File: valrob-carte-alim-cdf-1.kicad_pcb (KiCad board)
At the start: 4 copper layers, 87 x 57 mm, 201 parts, among them J1 USB_C_Receptacle_USB2.0_14P, J10 Conn_01x02, J11 Conn_01x02, J12 Conn_01x02, J13 Conn_01x02, J14 Conn_01x02, J15 Conn_01x02, J16 Conn_01x02, J17 Conn_01x02, J18 Conn_01x02, J19 Conn_01x02, J2 Conn_01x02, J20 Conn_01x02, J21 Conn_01x02, J22 Conn_01x02, J3 Conn_01x04_Pin, J4 Conn_01x02, J5 Conn_01x02, J6 Conn_01x02, J7 Conn_01x02, J8 Conn_01x02, J9 Conn_01x02, SW1 SW_Push, SW2 SW_Push, SW3 SW_Push, U1 SN65HVD230, U10 TPS259472A, U11 TPS259472A, U12 TPS259472A, U2 ESP32-S3-WROOM-1, U3 TLV75733PDBV, U4 TPS56A37, U5 TPS56A37, U6 TPS259472A, U7 TPS259472A, U8 TPS259472A, U9 TPS259472A

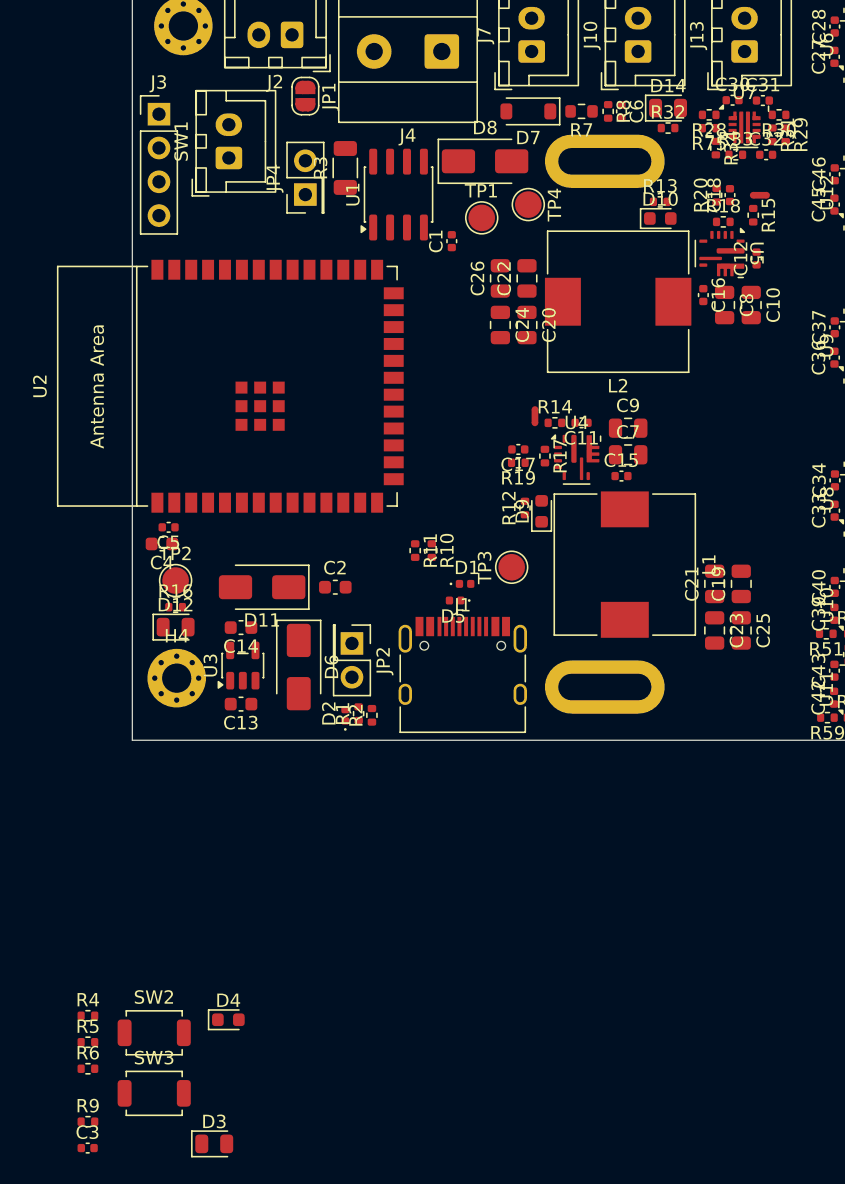
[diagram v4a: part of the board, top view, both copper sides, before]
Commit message: pcb: finish initial layout
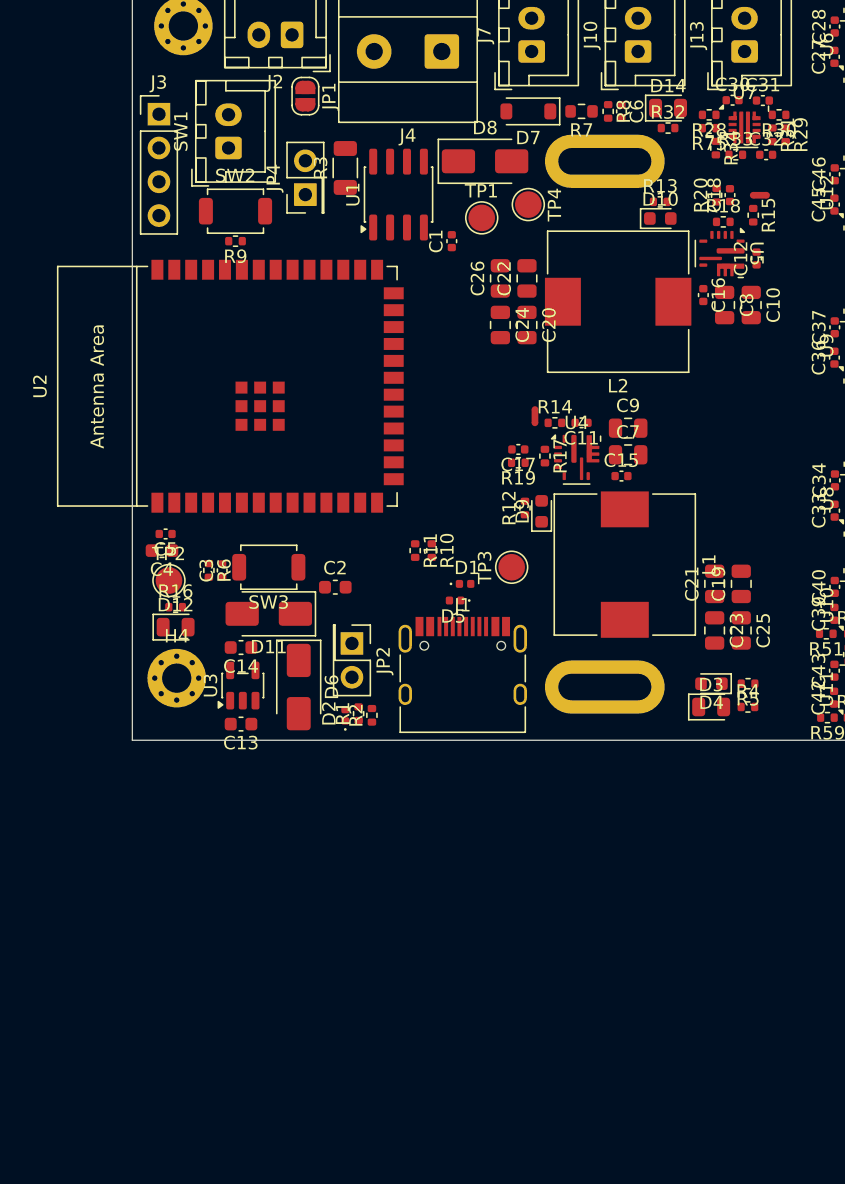
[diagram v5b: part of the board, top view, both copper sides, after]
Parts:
- moved R9 67.1 mm to (97.8, 72.5), turned to 180 degrees
- moved SW2 62.0 mm to (97.8, 70.2)
- moved R5 56.4 mm to (136.3, 105.8), turned to 180 degrees
- moved R4 54.7 mm to (136.2, 107.5)
- moved D3 49.7 mm to (133.5, 107.5)
- moved C3 44.6 mm to (96.8, 97.2), turned to 90 degrees
- moved D4 44.2 mm to (133.5, 105.8), turned to 180 degrees
- moved SW3 40.5 mm to (100.2, 97.0), turned to 180 degrees
- moved R6 38.5 mm to (95.8, 97.2), turned to -90 degrees
- moved D11 2.06 mm to (100.2, 100.5)
- moved C13 1.50 mm to (98.2, 108.8)
- moved C14 1.50 mm to (98.2, 103.0)
- moved D6 1.50 mm to (102.5, 106.0)
- moved U3 1.50 mm to (98.3, 105.9)
- moved SW1 0.75 mm to (97.2, 65.5)
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
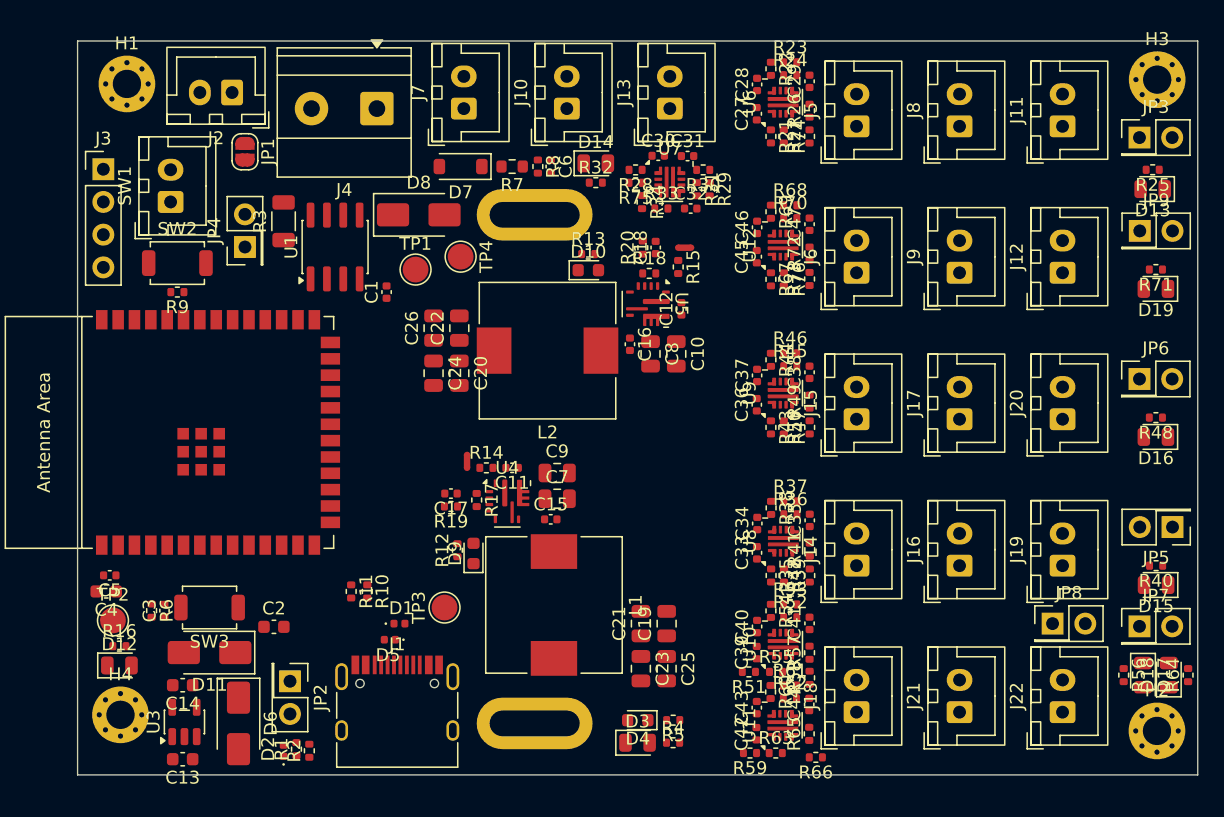
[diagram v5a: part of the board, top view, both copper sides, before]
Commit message: pcb: line up 2.54 headers
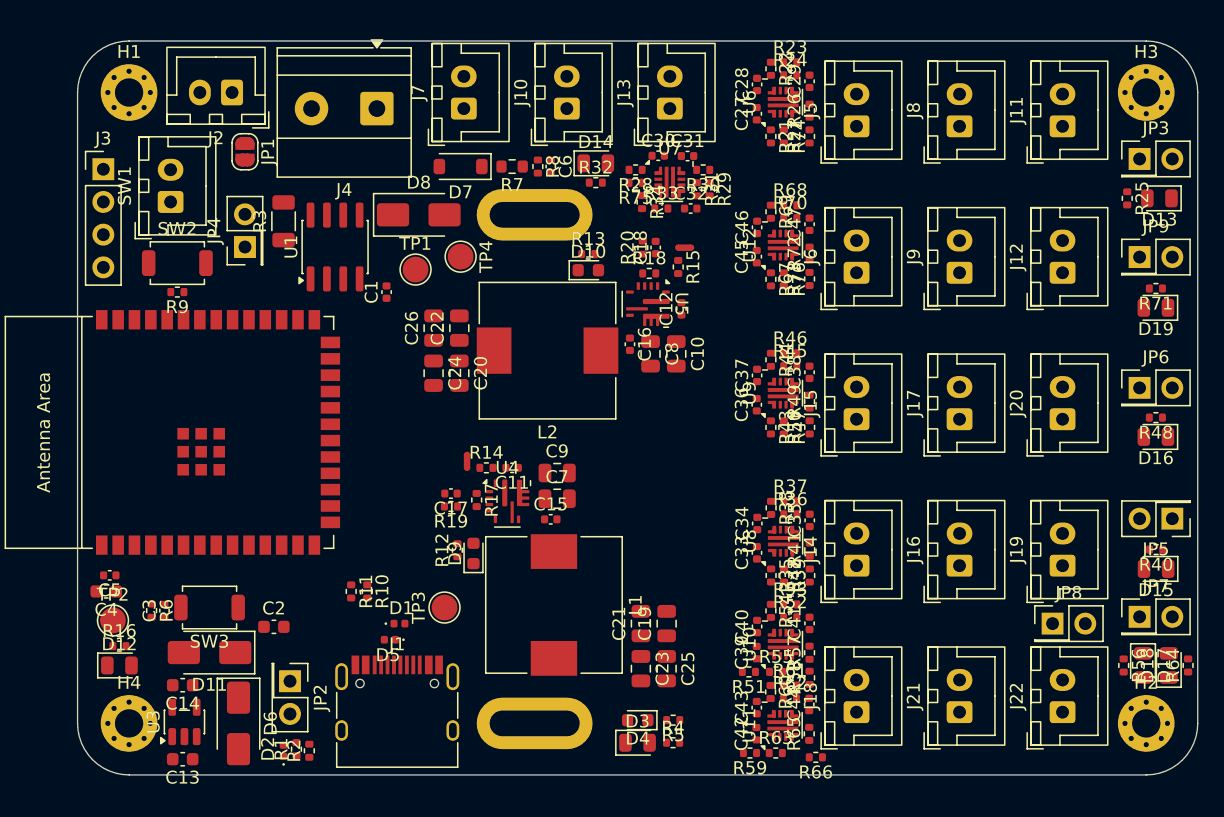
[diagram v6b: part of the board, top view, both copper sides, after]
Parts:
- moved R25 2.97 mm to (171.5, 65.2), turned to -90 degrees
- moved JP9 2.03 mm to (172.5, 69.8)
- moved JP3 1.66 mm to (172.5, 62.2)
- moved D19 1.47 mm to (173.8, 73.7)
- moved R71 1.47 mm to (173.8, 72.2)
- moved H3 1.31 mm to (173.0, 57.0)
- moved D15 1.25 mm to (173.8, 94.0)
- moved R40 1.25 mm to (173.8, 92.5)
- moved H2 1.02 mm to (173.0, 106.0)
- moved H4 0.94 mm to (94.0, 106.0)
- moved D13 0.89 mm to (174.0, 65.2)
- moved D17 0.75 mm to (172.8, 101.5)
- moved D18 0.75 mm to (174.8, 101.5)
- moved R56 0.75 mm to (171.2, 101.5)
- moved R64 0.75 mm to (176.2, 101.5)
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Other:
- outline, holes or cut-outs redrawn
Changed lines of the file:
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@@
 	(footprint "Resistor_SMD:R_0402_1005Metric"
 		(layer "F.Cu")
-		(at 173.765 93.75 180)
+		(at 173.765 92.5 180)
 		(descr "Resistor SMD 0402 (1005 Metric), square (rectangular) end terminal, IPC-7351 nominal, (Body size source: IPC-SM-782 page 72, https://www.pcb-3d.com/wordpress/wp-content/uploads/ipc-sm-782a_amendment_1_and_2.pdf), generated with kicad-footprint-generator")
 		(tags "resistor")
@@
 	(footprint "MountingHole:MountingHole_2.2mm_M2_Pad_Via"
 		(layer "F.Cu")
-		(at 173.85 56)
+		(at 173 57)
 		(descr "Mounting Hole 2.2mm, M2, generated by kicad-footprint-generator mountinghole.py")
 		(tags "mountinghole M2")
@@
 	(footprint "Connector_PinHeader_2.54mm:PinHeader_2x01_P2.54mm_Vertical"
 		(layer "F.Cu")
-		(at 172.475 79.25)
+		(at 172.484558 79.941668)
 		(descr "Through hole straight pin header, 2x01, 2.54mm pitch, double rows")
 		(tags "Through hole pin header THT 2x01 2.54mm double row")
@@
 	(footprint "LED_SMD:LED_0805_2012Metric"
 		(layer "F.Cu")
-		(at 173.5 64.5 180)
+		(at 174.024558 65.221668 180)
 		(descr "LED SMD 0805 (2012 Metric), square (rectangular) end terminal, IPC-7351 nominal, (Body size source: https://docs.google.com/spreadsheets/d/1BsfQQcO9C6DZCsRaXUlFlo91Tg2WpOkGARC1WS5S8t0/edit?usp=sharing), generated with kicad-footprint-generator")
 		(tags "LED")
@@
 	(footprint "Resistor_SMD:R_0402_1005Metric"
 		(layer "F.Cu")
-		(at 176.25 102.25 90)
+		(at 176.25 101.5 90)
 		(descr "Resistor SMD 0402 (1005 Metric), square (rectangular) end terminal, IPC-7351 nominal, (Body size source: IPC-SM-782 page 72, https://www.pcb-3d.com/wordpress/wp-content/uploads/ipc-sm-782a_amendment_1_and_2.pdf), generated with kicad-footprint-generator")
 		(tags "resistor")
@@
 	(footprint "LED_SMD:LED_0805_2012Metric"
 		(layer "F.Cu")
-		(at 173.765 95.25 180)
+		(at 173.765 94 180)
 		(descr "LED SMD 0805 (2012 Metric), square (rectangular) end terminal, IPC-7351 nominal, (Body size source: https://docs.google.com/spreadsheets/d/1BsfQQcO9C6DZCsRaXUlFlo91Tg2WpOkGARC1WS5S8t0/edit?usp=sharing), generated with kicad-footprint-generator")
 		(tags "LED")
@@
 	(footprint "MountingHole:MountingHole_2.2mm_M2_Pad_Via"
 		(layer "F.Cu")
-		(at 93.333274 105.333274)
+		(at 94 106)
 		(descr "Mounting Hole 2.2mm, M2, generated by kicad-footprint-generator mountinghole.py")
 		(tags "mountinghole M2")
@@
 	(footprint "LED_SMD:LED_0805_2012Metric"
 		(layer "F.Cu")
-		(at 173.75 72.25 180)
+		(at 173.75 73.721668 180)
 		(descr "LED SMD 0805 (2012 Metric), square (rectangular) end terminal, IPC-7351 nominal, (Body size source: https://docs.google.com/spreadsheets/d/1BsfQQcO9C6DZCsRaXUlFlo91Tg2WpOkGARC1WS5S8t0/edit?usp=sharing), generated with kicad-footprint-generator")
 		(tags "LED")
@@
 	(footprint "Connector_PinHeader_2.54mm:PinHeader_2x01_P2.54mm_Vertical"
 		(layer "F.Cu")
-		(at 172.475 98.46)
+		(at 172.484558 97.721668)
 		(descr "Through hole straight pin header, 2x01, 2.54mm pitch, double rows")
 		(tags "Through hole pin header THT 2x01 2.54mm double row")
@@
 	(footprint "LED_SMD:LED_0805_2012Metric"
 		(layer "F.Cu")
-		(at 174.75 102.25 90)
+		(at 174.75 101.5 90)
 		(descr "LED SMD 0805 (2012 Metric), square (rectangular) end terminal, IPC-7351 nominal, (Body size source: https://docs.google.com/spreadsheets/d/1BsfQQcO9C6DZCsRaXUlFlo91Tg2WpOkGARC1WS5S8t0/edit?usp=sharing), generated with kicad-footprint-generator")
 		(tags "LED")
@@
 	(footprint "Resistor_SMD:R_0402_1005Metric"
 		(layer "F.Cu")
-		(at 173.5 63 180)
+		(at 171.524558 65.221668 -90)
 		(descr "Resistor SMD 0402 (1005 Metric), square (rectangular) end terminal, IPC-7351 nominal, (Body size source: IPC-SM-782 page 72, https://www.pcb-3d.com/wordpress/wp-content/uploads/ipc-sm-782a_amendment_1_and_2.pdf), generated with kicad-footprint-generator")
 		(tags "resistor")
 		(property "Reference" "R25"
-			(at 0 -1.17 0)
+			(at 0 -1.17 90)
 			(layer "F.SilkS")
 			(effects
@@
 		)
 		(property "Value" "5k1"
-			(at 0 1.17 0)
+			(at 0 1.17 90)
 			(layer "F.Fab")
 			(effects
@@
 		)
 		(property "Datasheet" "~"
-			(at 0 0 0)
+			(at 0 0 90)
 			(layer "F.Fab")
 			(hide yes)
@@
 		)
 		(property "Description" "Resistor"
-			(at 0 0 0)
+			(at 0 0 90)
 			(layer "F.Fab")
 			(hide yes)
@@
 		)
 		(property "Manufacturer" "Uniroyal Elec"
-			(at 0 0 180)
+			(at 0 0 270)
 			(unlocked yes)
 			(layer "F.Fab")
@@
 		)
 		(property "Manufacturer Part Number" "0402WGF5101TCE"
-			(at 0 0 180)
+			(at 0 0 270)
 			(unlocked yes)
 			(layer "F.Fab")
@@
 		)
 		(property "Basic" "Y"
-			(at 0 0 180)
+			(at 0 0 270)
 			(unlocked yes)
 			(layer "F.Fab")
@@
 		)
 		(property "JLCPCB Part #" "C25905"
-			(at 0 0 180)
+			(at 0 0 270)
 			(unlocked yes)
 			(layer "F.Fab")
@@
 		)
 		(fp_text user "${REFERENCE}"
-			(at 0 0 0)
+			(at 0 0 90)
 			(layer "F.Fab")
 			(effects
@@
 		)
 		(pad "1" smd roundrect
-			(at -0.51 0 180)
+			(at -0.51 0 270)
 			(size 0.54 0.64)
 			(layers "F.Cu" "F.Mask" "F.Paste")
@@
 		)
 		(pad "2" smd roundrect
-			(at 0.51 0 180)
+			(at 0.51 0 270)
 			(size 0.54 0.64)
 			(layers "F.Cu" "F.Mask" "F.Paste")
@@
 	(footprint "Connector_PinHeader_2.54mm:PinHeader_2x01_P2.54mm_Vertical"
 		(layer "F.Cu")
-		(at 172.5 67.75)
+		(at 172.484558 69.781668)
 		(descr "Through hole straight pin header, 2x01, 2.54mm pitch, double rows")
 		(tags "Through hole pin header THT 2x01 2.54mm double row")
@@
 	(footprint "Connector_PinHeader_2.54mm:PinHeader_2x01_P2.54mm_Vertical"
 		(layer "F.Cu")
-		(at 172.475 60.5)
+		(at 172.484558 62.161668)
 		(descr "Through hole straight pin header, 2x01, 2.54mm pitch, double rows")
 		(tags "Through hole pin header THT 2x01 2.54mm double row")
@@
 	(footprint "Resistor_SMD:R_0402_1005Metric"
 		(layer "F.Cu")
-		(at 173.75 70.75 180)
+		(at 173.75 72.221668 180)
 		(descr "Resistor SMD 0402 (1005 Metric), square (rectangular) end terminal, IPC-7351 nominal, (Body size source: IPC-SM-782 page 72, https://www.pcb-3d.com/wordpress/wp-content/uploads/ipc-sm-782a_amendment_1_and_2.pdf), generated with kicad-footprint-generator")
 		(tags "resistor")
@@
 	(footprint "LED_SMD:LED_0805_2012Metric"
 		(layer "F.Cu")
-		(at 172.75 102.25 -90)
+		(at 172.75 101.5 -90)
 		(descr "LED SMD 0805 (2012 Metric), square (rectangular) end terminal, IPC-7351 nominal, (Body size source: https://docs.google.com/spreadsheets/d/1BsfQQcO9C6DZCsRaXUlFlo91Tg2WpOkGARC1WS5S8t0/edit?usp=sharing), generated with kicad-footprint-generator")
 		(tags "LED")
@@
 	(footprint "Connector_PinHeader_2.54mm:PinHeader_2x01_P2.54mm_Vertical"
 		(layer "F.Cu")
-		(at 175.04 90.75 180)
+		(at 175.024558 90.101668 180)
 		(descr "Through hole straight pin header, 2x01, 2.54mm pitch, double rows")
 		(tags "Through hole pin header THT 2x01 2.54mm double row")
@@
 	(footprint "MountingHole:MountingHole_2.2mm_M2_Pad_Via"
 		(layer "F.Cu")
-		(at 93.833274 56.333274)
+		(at 94 57)
 		(descr "Mounting Hole 2.2mm, M2, generated by kicad-footprint-generator mountinghole.py")
 		(tags "mountinghole M2")
@@
 	(footprint "Resistor_SMD:R_0402_1005Metric"
 		(layer "F.Cu")
-		(at 171.25 102.25 -90)
+		(at 171.25 101.5 -90)
 		(descr "Resistor SMD 0402 (1005 Metric), square (rectangular) end terminal, IPC-7351 nominal, (Body size source: IPC-SM-782 page 72, https://www.pcb-3d.com/wordpress/wp-content/uploads/ipc-sm-782a_amendment_1_and_2.pdf), generated with kicad-footprint-generator")
 		(tags "resistor")
@@
 	(footprint "MountingHole:MountingHole_2.2mm_M2_Pad_Via"
 		(layer "F.Cu")
-		(at 173.833274 106.583274)
+		(at 173 106)
 		(descr "Mounting Hole 2.2mm, M2, generated by kicad-footprint-generator mountinghole.py")
 		(tags "mountinghole M2")
@@
 		)
 	)
-	(gr_rect
-		(start 90 53)
-		(end 177 110)
+	(gr_arc
+		(start 177 106)
+		(mid 175.828427 108.828427)
+		(end 173 110)
+		(stroke
+			(width 0.05)
+			(type default)
+		)
+		(layer "Edge.Cuts")
+	)
+	(gr_arc
+		(start 94 110)
+		(mid 91.171573 108.828427)
+		(end 90 106)
+		(stroke
+			(width 0.05)
+			(type default)
+		)
+		(layer "Edge.Cuts")
+	)
+	(gr_line
+		(start 90 106)
+		(end 90 57)
+		(stroke
+			(width 0.05)
+			(type default)
+		)
+		(layer "Edge.Cuts")
+	)
+	(gr_line
+		(start 177 57)
+		(end 177 106)
+		(stroke
+			(width 0.05)
+			(type default)
+		)
+		(layer "Edge.Cuts")
+	)
+	(gr_arc
+		(start 173 53)
+		(mid 175.828427 54.171573)
+		(end 177 57)
+		(stroke
+			(width 0.05)
+			(type default)
+		)
+		(layer "Edge.Cuts")
+	)
+	(gr_line
+		(start 173 110)
+		(end 94 110)
+		(stroke
+			(width 0.05)
+			(type default)
+		)
+		(layer "Edge.Cuts")
+	)
+	(gr_line
+		(start 94 53)
+		(end 173 53)
+		(stroke
+			(width 0.05)
+			(type default)
+		)
+		(layer "Edge.Cuts")
+	)
+	(gr_arc
+		(start 90 57)
+		(mid 91.171573 54.171573)
+		(end 94 53)
 		(stroke
 			(width 0.05)
 			(type default)
 		)
-		(fill no)
 		(layer "Edge.Cuts")
 	)
